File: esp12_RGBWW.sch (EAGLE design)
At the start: 34 parts, among them Q1 AOD2910SMD, Q2 AOD2910SMD, Q3 AOD2910SMD, Q4 AOD2910SMD, Q5 AOD2910SMD, U1 TPS5410DR

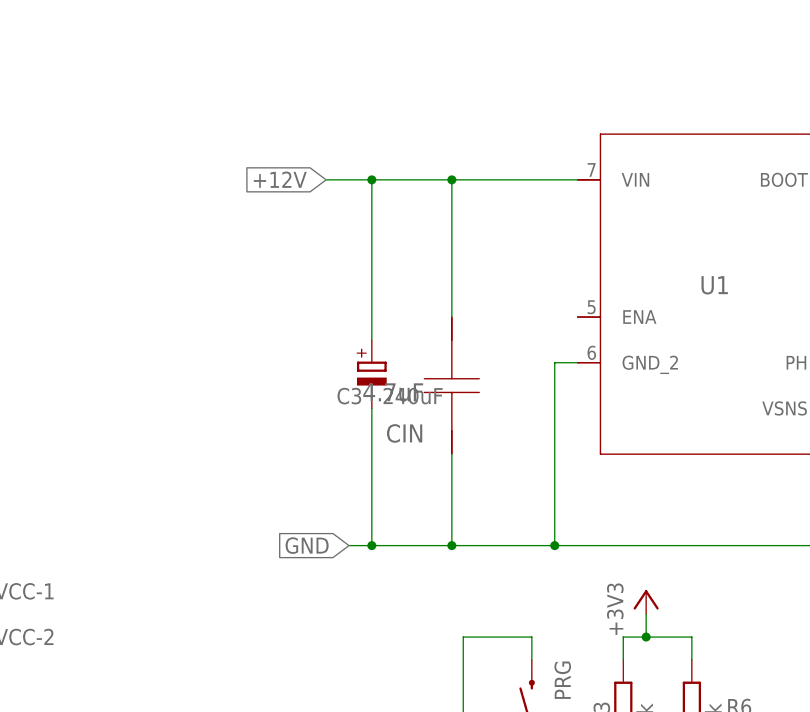
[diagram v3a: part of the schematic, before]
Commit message: added enable function
I added a pin header to short the TPS5410's ENABLE pin to GND, thus switching off the DC/DC converter, effectively turning the controller completely off.
The controller should function normally, when this is left open. Including a switch that connects those two pins is a way of switching the controller off without disconnecting the 12V supply. Whatever it'll be good for.
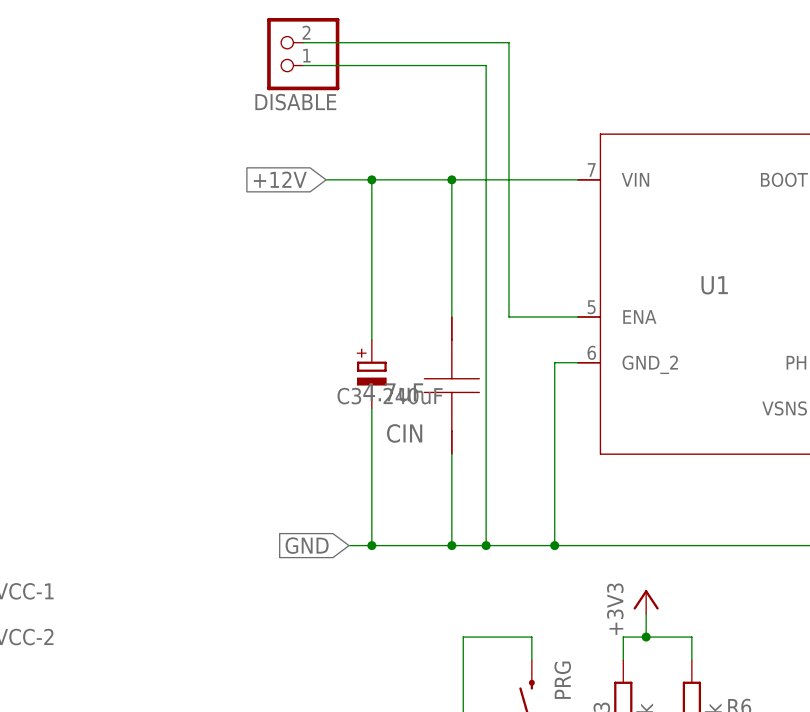
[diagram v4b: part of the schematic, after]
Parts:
- added DISABLE: (no value), pinhead:PINHD-1X2
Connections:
- new net ENA: DISABLE.2, U1.ENA
- net GND: now also DISABLE.1
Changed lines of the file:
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@@
 <grid distance="0.1" unitdist="inch" unit="inch" style="lines" multiple="1" display="no" altdistance="0.01" altunitdist="inch" altunit="inch"/>
 <layers>
-<layer number="1" name="Top" color="4" fill="1" visible="yes" active="no"/>
-<layer number="16" name="Bottom" color="1" fill="1" visible="yes" active="no"/>
-<layer number="17" name="Pads" color="2" fill="1" visible="yes" active="no"/>
-<layer number="18" name="Vias" color="2" fill="1" visible="yes" active="no"/>
-<layer number="19" name="Unrouted" color="6" fill="1" visible="yes" active="no"/>
-<layer number="20" name="Dimension" color="15" fill="1" visible="yes" active="no"/>
-<layer number="21" name="tPlace" color="7" fill="1" visible="yes" active="no"/>
-<layer number="22" name="bPlace" color="7" fill="1" visible="yes" active="no"/>
-<layer number="23" name="tOrigins" color="15" fill="1" visible="yes" active="no"/>
-<layer number="24" name="bOrigins" color="15" fill="1" visible="yes" active="no"/>
-<layer number="25" name="tNames" color="7" fill="1" visible="yes" active="no"/>
-<layer number="26" name="bNames" color="7" fill="1" visible="yes" active="no"/>
-<layer number="27" name="tValues" color="7" fill="1" visible="yes" active="no"/>
-<layer number="28" name="bValues" color="7" fill="1" visible="yes" active="no"/>
+<layer number="1" name="Top" color="4" fill="1" visible="no" active="no"/>
+<layer number="16" name="Bottom" color="1" fill="1" visible="no" active="no"/>
+<layer number="17" name="Pads" color="2" fill="1" visible="no" active="no"/>
+<layer number="18" name="Vias" color="2" fill="1" visible="no" active="no"/>
+<layer number="19" name="Unrouted" color="6" fill="1" visible="no" active="no"/>
+<layer number="20" name="Dimension" color="15" fill="1" visible="no" active="no"/>
+<layer number="21" name="tPlace" color="7" fill="1" visible="no" active="no"/>
+<layer number="22" name="bPlace" color="7" fill="1" visible="no" active="no"/>
+<layer number="23" name="tOrigins" color="15" fill="1" visible="no" active="no"/>
+<layer number="24" name="bOrigins" color="15" fill="1" visible="no" active="no"/>
+<layer number="25" name="tNames" color="7" fill="1" visible="no" active="no"/>
+<layer number="26" name="bNames" color="7" fill="1" visible="no" active="no"/>
+<layer number="27" name="tValues" color="7" fill="1" visible="no" active="no"/>
+<layer number="28" name="bValues" color="7" fill="1" visible="no" active="no"/>
 <layer number="29" name="tStop" color="7" fill="3" visible="no" active="no"/>
 <layer number="30" name="bStop" color="7" fill="6" visible="no" active="no"/>
@@
 <layer number="35" name="tGlue" color="7" fill="4" visible="no" active="no"/>
 <layer number="36" name="bGlue" color="7" fill="5" visible="no" active="no"/>
-<layer number="37" name="tTest" color="7" fill="1" visible="yes" active="no"/>
-<layer number="38" name="bTest" color="7" fill="1" visible="yes" active="no"/>
+<layer number="37" name="tTest" color="7" fill="1" visible="no" active="no"/>
+<layer number="38" name="bTest" color="7" fill="1" visible="no" active="no"/>
 <layer number="39" name="tKeepout" color="4" fill="11" visible="no" active="no"/>
 <layer number="40" name="bKeepout" color="1" fill="11" visible="no" active="no"/>
@@
 <layer number="44" name="Drills" color="7" fill="1" visible="no" active="no"/>
 <layer number="45" name="Holes" color="7" fill="1" visible="no" active="no"/>
-<layer number="46" name="Milling" color="3" fill="1" visible="yes" active="no"/>
-<layer number="47" name="Measures" color="7" fill="1" visible="yes" active="no"/>
-<layer number="48" name="Document" color="7" fill="1" visible="yes" active="no"/>
-<layer number="49" name="Reference" color="7" fill="1" visible="yes" active="no"/>
-<layer number="50" name="dxf" color="7" fill="1" visible="yes" active="no"/>
-<layer number="51" name="tDocu" color="7" fill="1" visible="yes" active="no"/>
-<layer number="52" name="bDocu" color="7" fill="1" visible="yes" active="no"/>
-<layer number="53" name="tGND_GNDA" color="7" fill="9" visible="yes" active="no"/>
-<layer number="54" name="bGND_GNDA" color="1" fill="9" visible="yes" active="no"/>
-<layer number="56" name="wert" color="7" fill="1" visible="yes" active="no"/>
-<layer number="57" name="tCAD" color="7" fill="1" visible="yes" active="no"/>
-<layer number="59" name="tCarbon" color="7" fill="1" visible="yes" active="no"/>
-<layer number="60" name="bCarbon" color="7" fill="1" visible="yes" active="no"/>
+<layer number="46" name="Milling" color="3" fill="1" visible="no" active="no"/>
+<layer number="47" name="Measures" color="7" fill="1" visible="no" active="no"/>
+<layer number="48" name="Document" color="7" fill="1" visible="no" active="no"/>
+<layer number="49" name="Reference" color="7" fill="1" visible="no" active="no"/>
+<layer number="50" name="dxf" color="7" fill="1" visible="no" active="no"/>
+<layer number="51" name="tDocu" color="7" fill="1" visible="no" active="no"/>
+<layer number="52" name="bDocu" color="7" fill="1" visible="no" active="no"/>
+<layer number="53" name="tGND_GNDA" color="7" fill="9" visible="no" active="no"/>
+<layer number="54" name="bGND_GNDA" color="1" fill="9" visible="no" active="no"/>
+<layer number="56" name="wert" color="7" fill="1" visible="no" active="no"/>
+<layer number="57" name="tCAD" color="7" fill="1" visible="no" active="no"/>
+<layer number="59" name="tCarbon" color="7" fill="1" visible="no" active="no"/>
+<layer number="60" name="bCarbon" color="7" fill="1" visible="no" active="no"/>
 <layer number="90" name="Modules" color="5" fill="1" visible="yes" active="yes"/>
 <layer number="91" name="Nets" color="2" fill="1" visible="yes" active="yes"/>
@@
 <part name="C3" library="resistor" deviceset="CPOL-EU" device="E2.5-7" value="240uF"/>
 <part name="PROG" library="con-lstb" deviceset="MA03-1" device=""/>
+<part name="DISABLE" library="pinhead" deviceset="PINHD-1X2" device=""/>
 </parts>
 <sheets>
@@
 </instance>
 <instance part="PROG" gate="G$1" x="2.54" y="50.8"/>
+<instance part="DISABLE" gate="G$1" x="-5.08" y="139.7" rot="R180"/>
 </instances>
 <busses>
@@
 <wire x1="2.54" y1="83.82" x2="5.08" y2="83.82" width="0.1524" layer="91"/>
 <wire x1="5.08" y1="83.82" x2="13.97" y2="83.82" width="0.1524" layer="91"/>
-<wire x1="13.97" y1="83.82" x2="25.4" y2="83.82" width="0.1524" layer="91"/>
+<wire x1="13.97" y1="83.82" x2="17.78" y2="83.82" width="0.1524" layer="91"/>
+<wire x1="17.78" y1="83.82" x2="25.4" y2="83.82" width="0.1524" layer="91"/>
 <wire x1="25.4" y1="83.82" x2="78.74" y2="83.82" width="0.1524" layer="91"/>
 <wire x1="78.74" y1="83.82" x2="91.44" y2="83.82" width="0.1524" layer="91"/>
@@
 <wire x1="5.08" y1="99.06" x2="5.08" y2="83.82" width="0.1524" layer="91"/>
 <junction x="5.08" y="83.82"/>
+<pinref part="DISABLE" gate="G$1" pin="1"/>
+<wire x1="-2.54" y1="137.16" x2="17.78" y2="137.16" width="0.1524" layer="91"/>
+<wire x1="17.78" y1="137.16" x2="17.78" y2="83.82" width="0.1524" layer="91"/>
+<junction x="17.78" y="83.82"/>
 </segment>
 <segment>
@@
 </segment>
 </net>
+<net name="ENA" class="0">
+<segment>
+<pinref part="DISABLE" gate="G$1" pin="2"/>
+<wire x1="-2.54" y1="139.7" x2="20.32" y2="139.7" width="0.1524" layer="91"/>
+<pinref part="U1" gate="A" pin="ENA"/>
+<wire x1="20.32" y1="139.7" x2="20.32" y2="109.22" width="0.1524" layer="91"/>
+<wire x1="20.32" y1="109.22" x2="27.94" y2="109.22" width="0.1524" layer="91"/>
+</segment>
+</net>

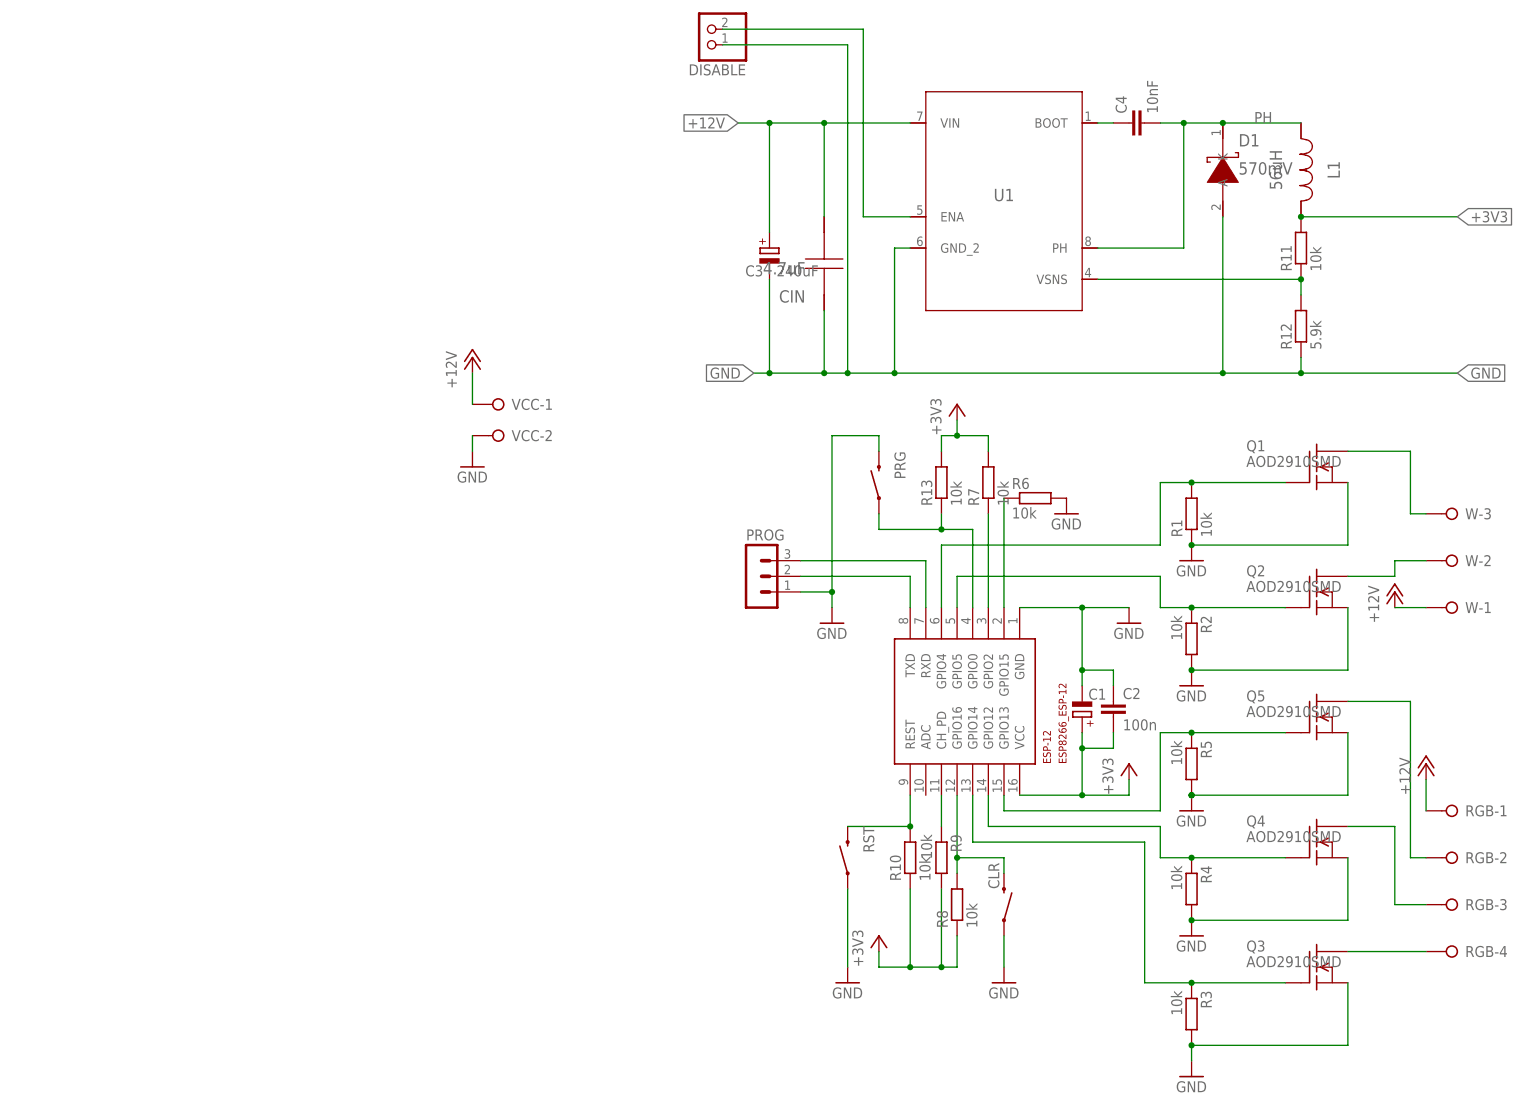
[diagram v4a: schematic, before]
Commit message: some power supply improvements
added a snubber network to PH (140MHz) plus a 10nF cap on the +3V3 line
Added low impedance floodfills for +3V3 and PH where applicable
switched the location of the RST and PRG switches since it seems easier to have the RST on the outside
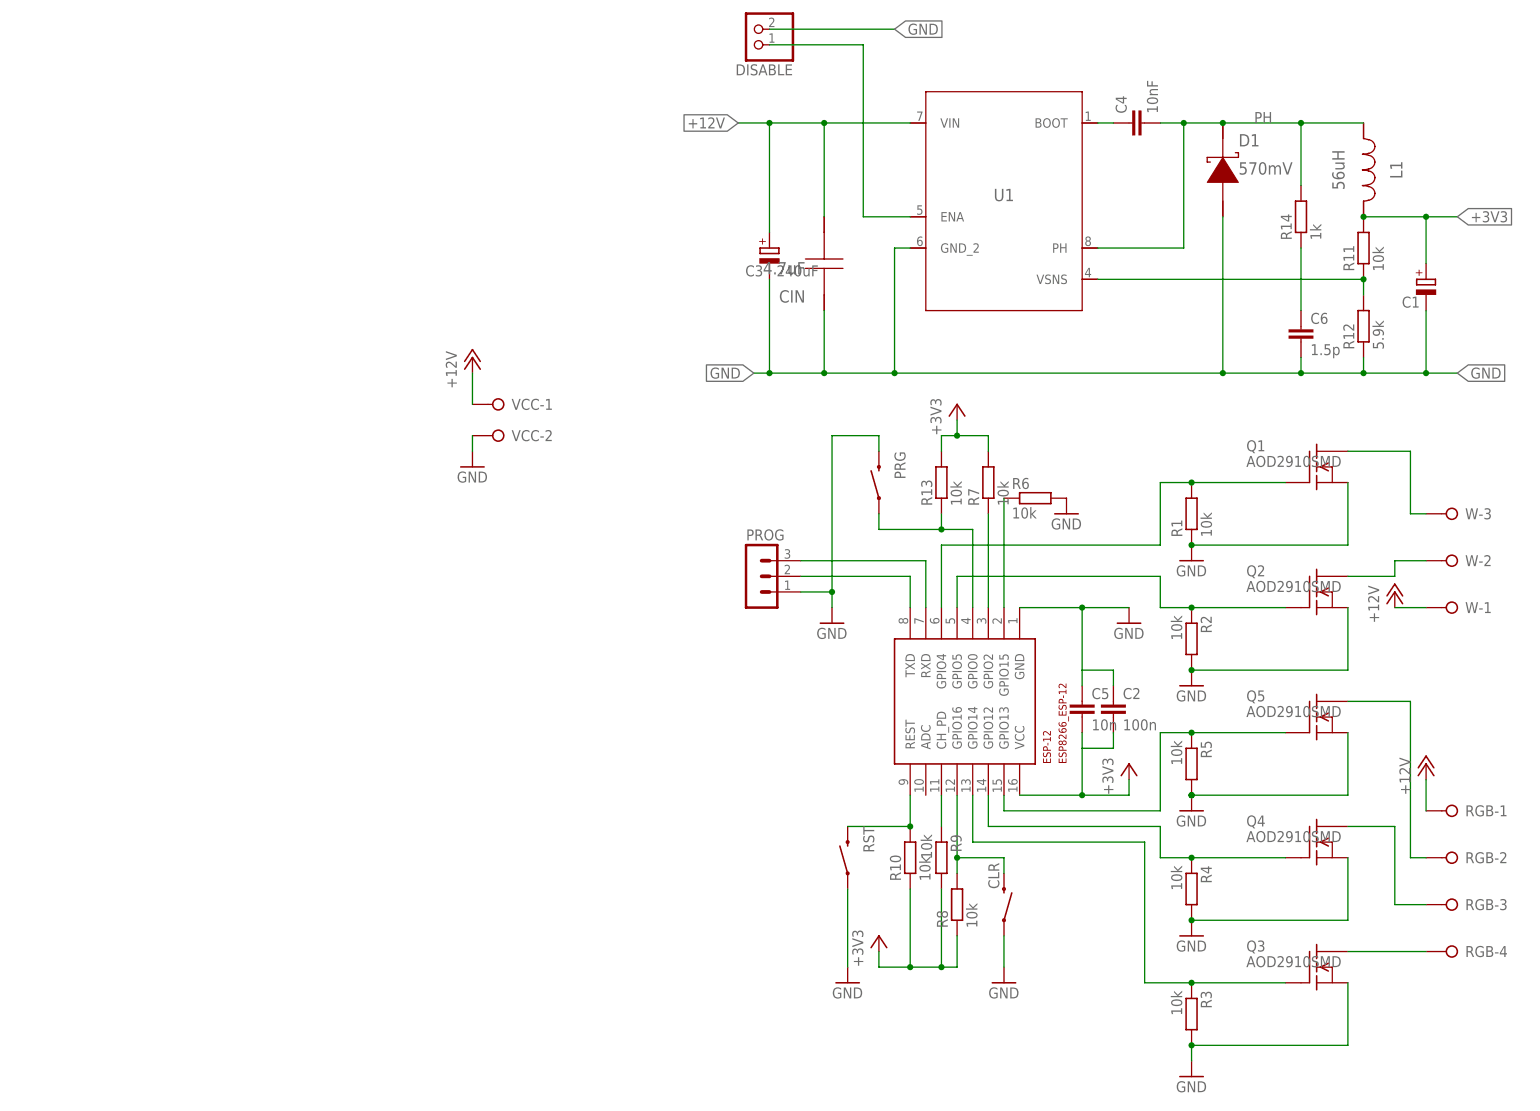
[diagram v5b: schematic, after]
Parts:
- added C5: 10n, rcl:C-EUC0805
- added C6: 1.5p, rcl:C-EUC0805
- added R14: 1k, rcl:R-EU_R0805
- D1: device AcceleratedDesigns_Lib:PMEG6010CEH,115 -> TI_Accelerated_Design_neu:B160-13-F
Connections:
- new net SNUB: C6.1, R14.1
- net +3V3: now also C5.2
- net ENA: now also DISABLE.1; no longer DISABLE.2
- net GND: now also C5.1, C6.2, DISABLE.2; no longer DISABLE.1
- net PH: now also R14.2
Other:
- moved on the sheet: C1, DISABLE, L1, R11, R12
